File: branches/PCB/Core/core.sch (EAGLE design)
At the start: 16 parts, among them U1 PIC32MX230F064B-

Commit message: Completed Core Schematic
Needs to check schematic and create layout
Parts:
- added 3V3_VREG: (no value), SparkFun-PowerIC:V_REG_78XX-TO-220
- added BARREL_JACK: (no value), adafruit:DCBARRELPTH
- added PORTA: (no value), SparkFun-Connectors:M05PTH
- added PORTB: M16PTH, SparkFun-Connectors:M16PTH
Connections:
- new net N$2: 3V3_VREG.IN, BARREL_JACK.PWR
- new net N$8: 3V3_VREG.GND, BARREL_JACK.GND
- new net RB0: PORTB.1, U1.PGED1/AN2/C1IND/C2INB/C3IND/RPB0/PMD0/RB0
- new net RB1: PORTB.2, U1.PGEC1/AN3/C1INC/C2INA/RPB1/CTED12/PMD1/RB1
- new net RB13: PORTB.14, U1.AN11/RPB13/CTPLS/PMRD/RB13
- new net RB14: PORTB.15, U1.CVREF/AN10/C3INB/RPB14/VBUSON/SCK1/CTED5/RB14
- new net RB15: PORTB.16, U1.AN9/C3INA/RPB15/SCK2/CTED6/PMCS1/RB15
- new net RB2: PORTB.3, U1.AN4/C1INB/C2IND/RPB2/SDA2/CTED13/PMD2/RB2
- new net RB3: PORTB.4, U1.AN5/C1INA/C2INC/RTCC/RPB3/SCL2/PMWR/RB3
- new net RB4: PORTB.5, U1.SOSCI/RPB4/RB4
- new net RB5: PORTB.6, U1.TMS/RPB5/USBID/RB5
- new net RB7: PORTB.8, U1.TDI/RPB7/CTED3/PMD5/INT0/RB7
- new net RB8: PORTB.9, U1.TCK/RPB8/SCL1/CTED10/PMD4/RB8
- new net RB9: PORTB.10, U1.TDO/RPB9/SDA1/CTED4/PMD3/RB9
- net D+: now also PORTB.11
- net D-: now also PORTB.12
- net OSC1: now also PORTA.3
- net OSC2: now also PORTA.4
- net RA0: now also PORTA.1
- net RA1: now also PORTA.2
- net RA4: now also PORTA.5
- net VDD: now also 3V3_VREG.OUT
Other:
- note added: "<-- PORTS -->"
- moved on the sheet: BOOTLOADER, C1, C2, C3, C4, C5, CRYSTAL1, PICKIT3, PWR_LED, R1, R2, R3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

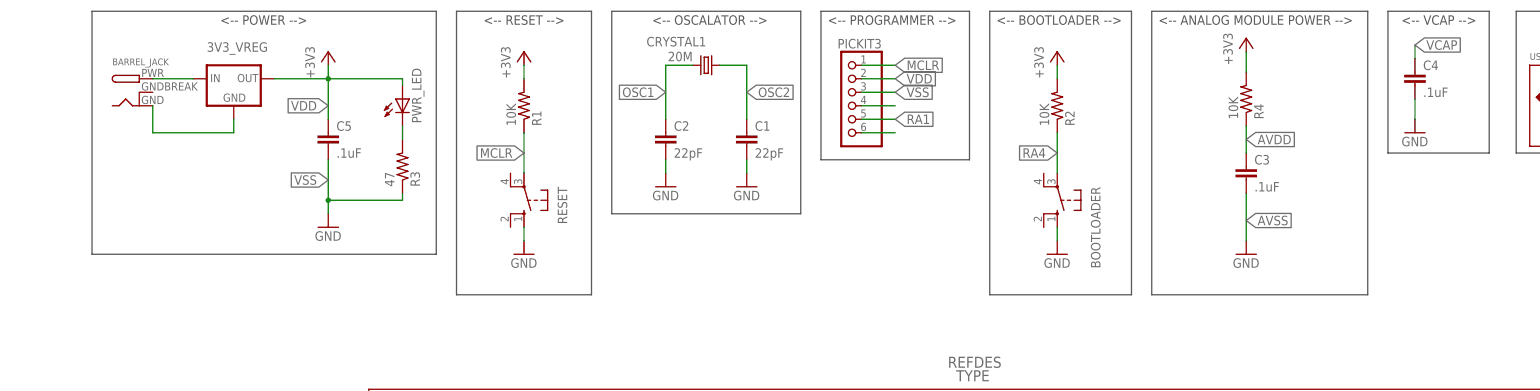
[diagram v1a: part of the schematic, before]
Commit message: Working on Routing
Going to try simplifying VSS / GND
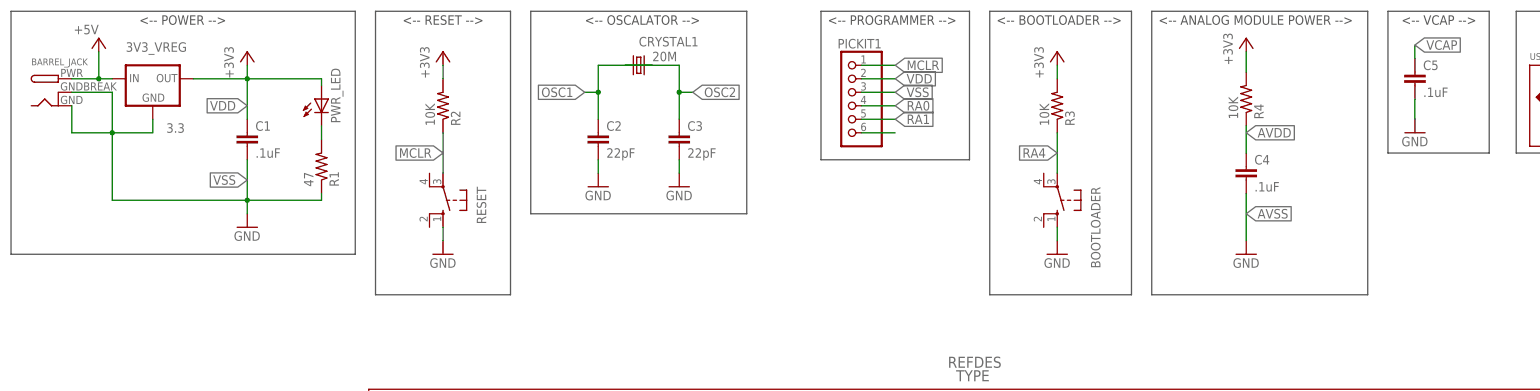
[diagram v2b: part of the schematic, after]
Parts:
- 3V3_VREG: value (none) -> 3.3
- C1: value 22pF -> .1uF
- C3: value .1uF -> 22pF
- R1: value 10K -> 47
- R3: value 47 -> 10K
- renumbered PICKIT3 to PICKIT1
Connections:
- net N$2 renamed +5V
- removed net N$1: C1.1, CRYSTAL1.1
- removed net N$3: PICKIT1.2, PICKIT1.3, PICKIT1.4, PICKIT1.5, PICKIT1.6
- removed net N$4: C2.1, CRYSTAL1.2
- removed net N$6: C4.1
- removed net N$7: C3.1, R4.1
- removed net N$8: 3V3_VREG.GND, BARREL_JACK.GND
- net +3V3: now also R3.2; no longer R1.2
- net AVDD: now also C4.1, R4.1
- net AVSS: now also C4.2
- net GND: now also C5.2; no longer C1.2, C4.2
- net MCLR: now also R2.1; no longer R1.1
- net N$5: now also R1.2; no longer R3.2
- net OSC1: now also C2.1, CRYSTAL1.2
- net OSC2: now also C3.1, CRYSTAL1.1
- net RA0: now also PICKIT1.2, PICKIT1.3, PICKIT1.4, PICKIT1.5, PICKIT1.6
- net RA4: now also R3.1; no longer R2.1
- net VCAP: now also C5.1
- net VDD: now also C1.1; no longer C5.1
- net VSS: now also 3V3_VREG.GND, BARREL_JACK.GND, BARREL_JACK.GNDBREAK, C1.2, R1.1; no longer C5.2, R3.1
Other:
- moved on the sheet: 3V3_VREG, BARREL_JACK, C1, C2, C3, C4, C5, CRYSTAL1, PWR_LED, R1, R2, R3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

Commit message: Pre Gerber for Rev 1.00
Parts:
- added POWER: (no value), adafruit:PINHD-2X4
- renumbered BOOTLOADER to BTLDR, PICKIT1 to PICKIT3
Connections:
- removed net VDD: 3V3_VREG.OUT, C1.1, PWR_LED.A, U1.VDD, U1.VUSB3V3
- removed net VSS: 3V3_VREG.GND, BARREL_JACK.GND, BARREL_JACK.GNDBREAK, C1.2, R1.1, U1.VSS, U1.VSS_2, USB_MINI_B.GND
- net +3V3: now also 3V3_VREG.OUT, C1.1, PICKIT3.2, POWER.3, POWER.4, PWR_LED.A, U1.VDD, U1.VUSB3V3
- net +5V: now also POWER.1, POWER.2
- net D-: now also USB_MINI_B.ID; no longer USB_MINI_B.D-
- net GND: now also 3V3_VREG.GND, BARREL_JACK.GND, BARREL_JACK.GNDBREAK, C1.2, PICKIT3.3, POWER.5, POWER.6, POWER.7, POWER.8, R1.1, U1.VSS, U1.VSS_2, USB_MINI_B.VBUS
- net RA0: no longer PICKIT3.2, PICKIT3.3, PICKIT3.5, PICKIT3.6
- net RA1: now also PICKIT3.5
- net VBUS: now also USB_MINI_B.GND; no longer USB_MINI_B.VBUS
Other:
- moved on the sheet: 3V3_VREG, BARREL_JACK, C1, PWR_LED, R1

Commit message: Minor Updates
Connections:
- net GND: now also USB_MINI_B.GND; no longer USB_MINI_B.VBUS
- net VBUS: now also USB_MINI_B.VBUS; no longer USB_MINI_B.GND
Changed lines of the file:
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@@
 <instance part="GND12" gate="1" x="284.48" y="40.64"/>
 <instance part="+3V8" gate="G$1" x="-25.4" y="43.18"/>
-<instance part="GND10" gate="1" x="271.78" y="129.54"/>
+<instance part="GND10" gate="1" x="264.16" y="119.38"/>
 </instances>
 <busses>
@@
 </segment>
 <segment>
-<pinref part="USB_MINI_B" gate="G$1" pin="VBUS"/>
+<pinref part="USB_MINI_B" gate="G$1" pin="GND"/>
 <pinref part="GND10" gate="1" pin="GND"/>
-<wire x1="259.08" y1="132.08" x2="271.78" y2="132.08" width="0.1524" layer="91"/>
+<wire x1="259.08" y1="121.92" x2="264.16" y2="121.92" width="0.1524" layer="91"/>
 </segment>
 </net>
@@
 </segment>
 <segment>
-<pinref part="USB_MINI_B" gate="G$1" pin="GND"/>
-<wire x1="259.08" y1="121.92" x2="261.62" y2="121.92" width="0.1524" layer="91"/>
-<label x="261.62" y="121.92" size="1.778" layer="95" xref="yes"/>
-</segment>
-</net>
+<pinref part="USB_MINI_B" gate="G$1" pin="VBUS"/>
+<wire x1="259.08" y1="132.08" x2="259.08" y2="134.62" width="0.1524" layer="91"/>
+<wire x1="259.08" y1="134.62" x2="261.62" y2="134.62" width="0.1524" layer="91"/>
+<label x="261.62" y="134.62" size="1.778" layer="95" xref="yes"/>
+</segment>
+</net>
